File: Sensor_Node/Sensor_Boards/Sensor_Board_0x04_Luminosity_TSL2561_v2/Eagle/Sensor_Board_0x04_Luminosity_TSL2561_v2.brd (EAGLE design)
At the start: 55 x 35 mm, 20 parts, among them J1 M04_SMD_90, J4 ARDUINO_ISP, U1 MIKE-TEMP_TSL2561FN, U2 ATMEGA328P_TQFP, Y1 8MHZ

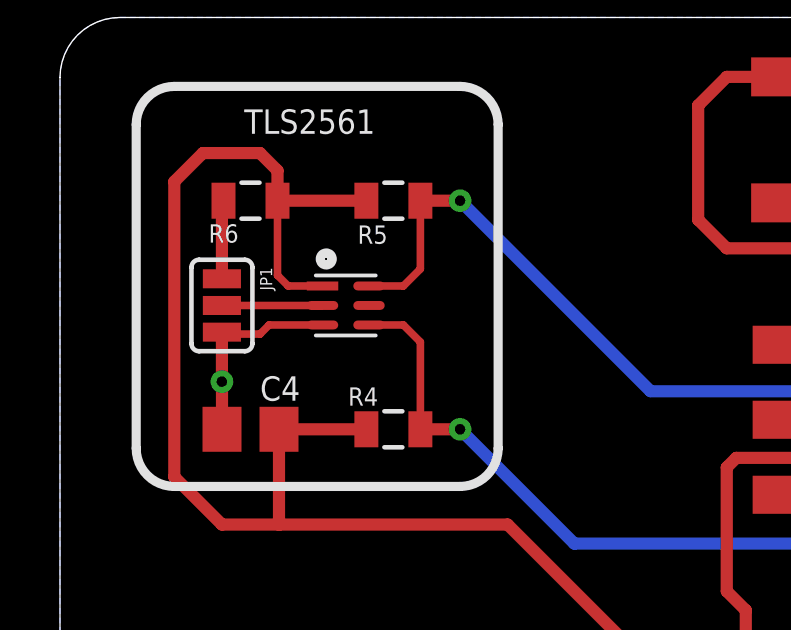
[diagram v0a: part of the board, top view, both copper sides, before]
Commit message: Various changes
- updated two masks
- changed combined mask again
- tiedied up CO2 sensor a bit
- used another footprint for TSL2561-sensor
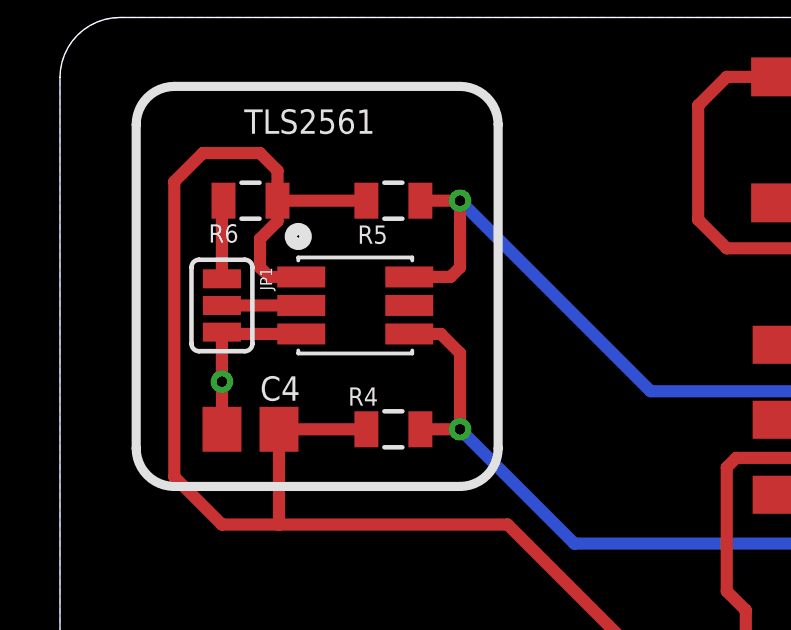
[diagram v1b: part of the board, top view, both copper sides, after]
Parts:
- removed U1: MIKE-TEMP_TSL2561FN, TSL2561 Luminosity Sensor BOB:MIKE-TEMP_FN-6
- added U3: MIKE-TEMP_TSL2561T, TSL2561 Luminosity Sensor BOB:MIKE-TEMP_TMB-6
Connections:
- net GND: now also U3.3; no longer U1.3
- net N$7: now also U3.2; no longer U1.2
- net SCL: now also U3.4; no longer U1.4
- net SDA: now also U3.6; no longer U1.6
- net VCC: now also U3.1; no longer U1.1
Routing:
- net GND: track 62.7 -> 62.0 mm
- net N$7: track 3.35 -> 2.65 mm
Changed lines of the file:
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@@
 <?xml version="1.0" encoding="utf-8"?>
 <!DOCTYPE eagle SYSTEM "eagle.dtd">
-<eagle version="8.5.0">
+<eagle version="8.5.2">
 <drawing>
 <settings>
@@
 <attribute name="SPICEPREFIX" value="C" x="36.83" y="25.4" size="1.778" layer="27" rot="R180" display="off"/>
 </element>
-<element name="U1" library="TSL2561 Luminosity Sensor BOB" package="MIKE-TEMP_FN-6" value="MIKE-TEMP_TSL2561FN" x="9.525" y="25.4" smashed="yes"/>
 <element name="R4" library="SparkFun-Passives" package="0805" value="10k" x="11.1125" y="21.2725" smashed="yes" rot="R180">
 <attribute name="NAME" x="10.6045" y="22.6695" size="0.6096" layer="25" rot="R180"/>
@@
 </element>
 <element name="JP1" library="TSL2561 Luminosity Sensor BOB" package="MIKE-TEMP_SJ_3" value="" x="5.3975" y="25.4" rot="R270"/>
+<element name="U3" library="TSL2561 Luminosity Sensor BOB" package="MIKE-TEMP_TMB-6" value="MIKE-TEMP_TSL2561T" x="9.8425" y="25.4" smashed="yes"/>
 </elements>
 <signals>
@@
 <wire x1="29.845" y1="25.7175" x2="29.845" y2="24.2475" width="0.4064" layer="1"/>
 <wire x1="29.845" y1="24.2475" x2="29.6875" y2="24.09" width="0.4064" layer="1"/>
-<contactref element="U1" pad="3"/>
 <contactref element="C4" pad="1"/>
 <contactref element="JP1" pad="3"/>
-<wire x1="5.461" y1="24.4475" x2="6.6675" y2="24.4475" width="0.254" layer="1"/>
 <wire x1="5.3975" y1="24.511" x2="5.461" y2="24.4475" width="0.254" layer="1"/>
 <wire x1="5.3975" y1="24.511" x2="5.4" y2="24.5085" width="0.4064" layer="1"/>
@@
 <wire x1="21.2725" y1="28.2575" x2="22.225" y2="27.305" width="0.4064" layer="1"/>
 <wire x1="22.225" y1="27.305" x2="28.2575" y2="27.305" width="0.4064" layer="1"/>
-<wire x1="8.75" y1="24.75" x2="6.97" y2="24.75" width="0.254" layer="1"/>
-<wire x1="6.97" y1="24.75" x2="6.6675" y2="24.4475" width="0.254" layer="1"/>
 <via x="5.3975" y="22.86" extent="1-16" drill="0.35"/>
 <wire x1="5.3975" y1="24.511" x2="5.3975" y2="22.86" width="0.4064" layer="1"/>
 <wire x1="5.3975" y1="22.86" x2="5.4" y2="22.8575" width="0.4064" layer="1"/>
 <wire x1="5.4" y1="22.8575" x2="5.4" y2="21.2725" width="0.4064" layer="1"/>
+<contactref element="U3" pad="3"/>
+<wire x1="8.0425" y1="24.45" x2="5.4585" y2="24.45" width="0.4064" layer="1"/>
+<wire x1="5.4585" y1="24.45" x2="5.3975" y2="24.511" width="0.4064" layer="1"/>
 </signal>
 <signal name="VCC" class="1">
@@
 <contactref element="R5" pad="2"/>
 <contactref element="R4" pad="2"/>
-<contactref element="U1" pad="1"/>
 <contactref element="R6" pad="2"/>
 <contactref element="C4" pad="2"/>
 <wire x1="10.2125" y1="28.8925" x2="7.25" y2="28.8925" width="0.4064" layer="1"/>
-<wire x1="8.75" y1="26.05" x2="7.605" y2="26.05" width="0.254" layer="1"/>
-<wire x1="7.25" y1="26.405" x2="7.25" y2="28.8925" width="0.254" layer="1"/>
-<wire x1="7.605" y1="26.05" x2="7.25" y2="26.405" width="0.254" layer="1"/>
 <wire x1="29.21" y1="11.43" x2="21.59" y2="11.43" width="0.4064" layer="1"/>
 <wire x1="14.9225" y1="18.0975" x2="7.3025" y2="18.0975" width="0.4064" layer="1"/>
@@
 <wire x1="3.81" y1="29.5275" x2="3.81" y2="19.685" width="0.4064" layer="1"/>
 <wire x1="7.25" y1="29.8975" x2="6.6675" y2="30.48" width="0.4064" layer="1"/>
+<contactref element="U3" pad="1"/>
+<wire x1="8.0425" y1="26.35" x2="6.9875" y2="26.35" width="0.4064" layer="1"/>
+<wire x1="6.6675" y1="26.67" x2="6.6675" y2="27.6225" width="0.4064" layer="1"/>
+<wire x1="6.6675" y1="27.6225" x2="7.25" y2="28.205" width="0.4064" layer="1"/>
+<wire x1="7.25" y1="28.205" x2="7.25" y2="28.8925" width="0.4064" layer="1"/>
+<wire x1="6.9875" y1="26.35" x2="6.6675" y2="26.67" width="0.4064" layer="1"/>
 </signal>
 <signal name="RESET">
@@
 <signal name="SCL">
 <contactref element="U2" pad="28"/>
-<contactref element="U1" pad="4"/>
 <contactref element="R4" pad="1"/>
-<wire x1="11.445" y1="24.75" x2="10.3" y2="24.75" width="0.254" layer="1"/>
-<wire x1="12.0125" y1="21.2725" x2="12.0125" y2="24.1825" width="0.254" layer="1"/>
-<wire x1="12.0125" y1="24.1825" x2="11.445" y2="24.75" width="0.254" layer="1"/>
 <wire x1="34.4424" y1="18.18" x2="33.5725" y2="18.18" width="0.4064" layer="1"/>
 <wire x1="33.5725" y1="18.18" x2="33.02" y2="18.7325" width="0.4064" layer="1"/>
@@
 <wire x1="17.145" y1="17.4625" x2="28.8925" y2="17.4625" width="0.4064" layer="16"/>
 <wire x1="13.335" y1="21.2725" x2="17.145" y2="17.4625" width="0.4064" layer="16"/>
+<contactref element="U3" pad="4"/>
+<wire x1="12.065" y1="21.325" x2="12.0125" y2="21.2725" width="0.3048" layer="1"/>
+<wire x1="11.6425" y1="24.45" x2="12.6975" y2="24.45" width="0.4064" layer="1"/>
+<wire x1="12.6975" y1="24.45" x2="13.335" y2="23.8125" width="0.4064" layer="1"/>
+<wire x1="13.335" y1="23.8125" x2="13.335" y2="21.2725" width="0.4064" layer="1"/>
 </signal>
 <signal name="SDA">
 <contactref element="U2" pad="27"/>
-<contactref element="U1" pad="6"/>
 <contactref element="R5" pad="1"/>
-<wire x1="11.445" y1="26.05" x2="10.3" y2="26.05" width="0.254" layer="1"/>
-<wire x1="12.0125" y1="28.8925" x2="12.0125" y2="26.6175" width="0.254" layer="1"/>
-<wire x1="12.0125" y1="26.6175" x2="11.445" y2="26.05" width="0.254" layer="1"/>
 <wire x1="34.4424" y1="18.98" x2="35.63" y2="18.98" width="0.4064" layer="1"/>
 <wire x1="35.63" y1="18.98" x2="36.195" y2="18.415" width="0.4064" layer="1"/>
@@
 <wire x1="13.335" y1="28.8925" x2="12.0125" y2="28.8925" width="0.4064" layer="1"/>
 <wire x1="19.685" y1="22.5425" x2="33.9725" y2="22.5425" width="0.4064" layer="16"/>
+<contactref element="U3" pad="6"/>
+<wire x1="11.6425" y1="26.35" x2="11.69625" y2="26.40375" width="0.3048" layer="1"/>
+<wire x1="11.69625" y1="26.40375" x2="11.7475" y2="26.455" width="0.3048" layer="1"/>
+<wire x1="12.065" y1="28.84" x2="12.0125" y2="28.8925" width="0.3048" layer="1"/>
+<wire x1="13.335" y1="28.8925" x2="13.335" y2="26.67" width="0.4064" layer="1"/>
+<wire x1="13.335" y1="26.67" x2="13.0175" y2="26.3525" width="0.4064" layer="1"/>
+<wire x1="13.0175" y1="26.3525" x2="11.7475" y2="26.3525" width="0.4064" layer="1"/>
+<wire x1="11.7475" y1="26.3525" x2="11.69625" y2="26.40375" width="0.4064" layer="1"/>
 </signal>
 <signal name="L1">
@@
 </signal>
 <signal name="N$7">
-<contactref element="U1" pad="2"/>
 <contactref element="JP1" pad="2"/>
-<wire x1="8.75" y1="25.4" x2="5.3975" y2="25.4" width="0.254" layer="1"/>
+<contactref element="U3" pad="2"/>
+<wire x1="5.3975" y1="25.4" x2="8.0425" y2="25.4" width="0.4064" layer="1"/>
 </signal>
 </signals>
